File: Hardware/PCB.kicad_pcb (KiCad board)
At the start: 2 copper layers, 53.4 x 22 mm, 13 parts, among them J2 Conn_01x06, SW1 SW_MEC_5E, U1 ME54BS01_V1.0, U2 MCP1700x-330xxTO

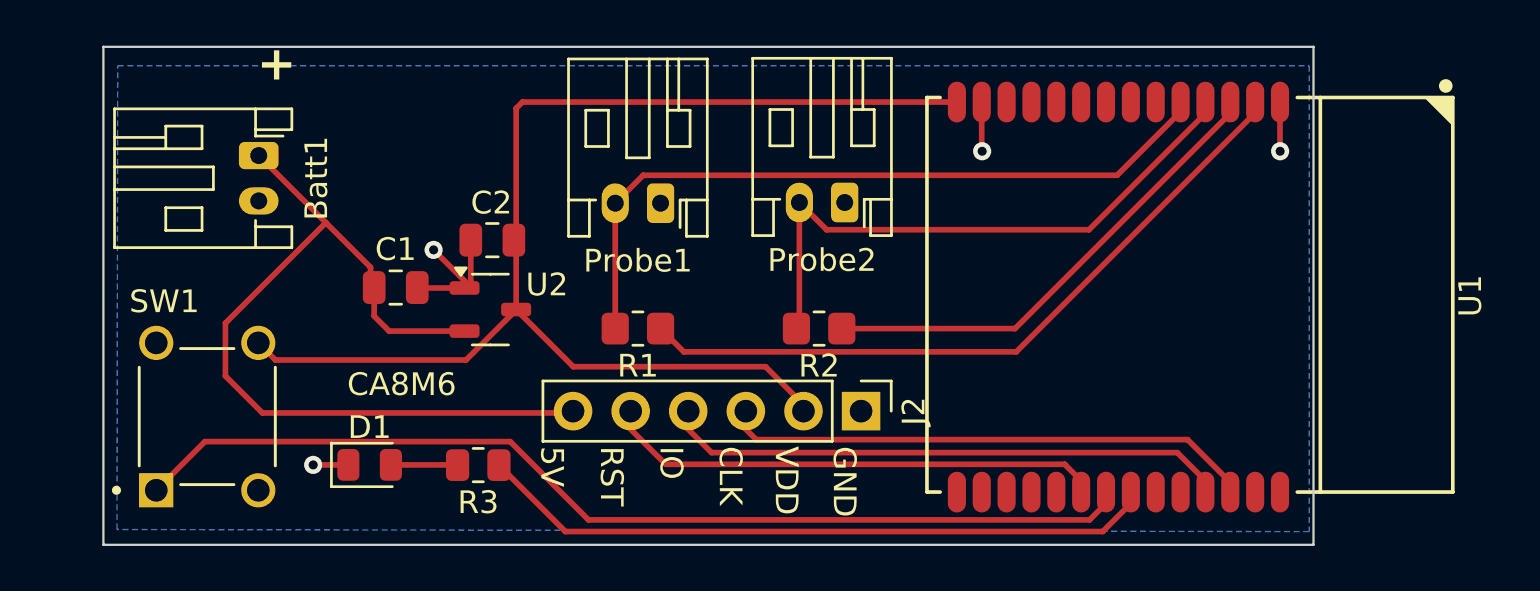
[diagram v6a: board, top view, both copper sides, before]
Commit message: Update PCB with fix for LDO and tracing improvements.
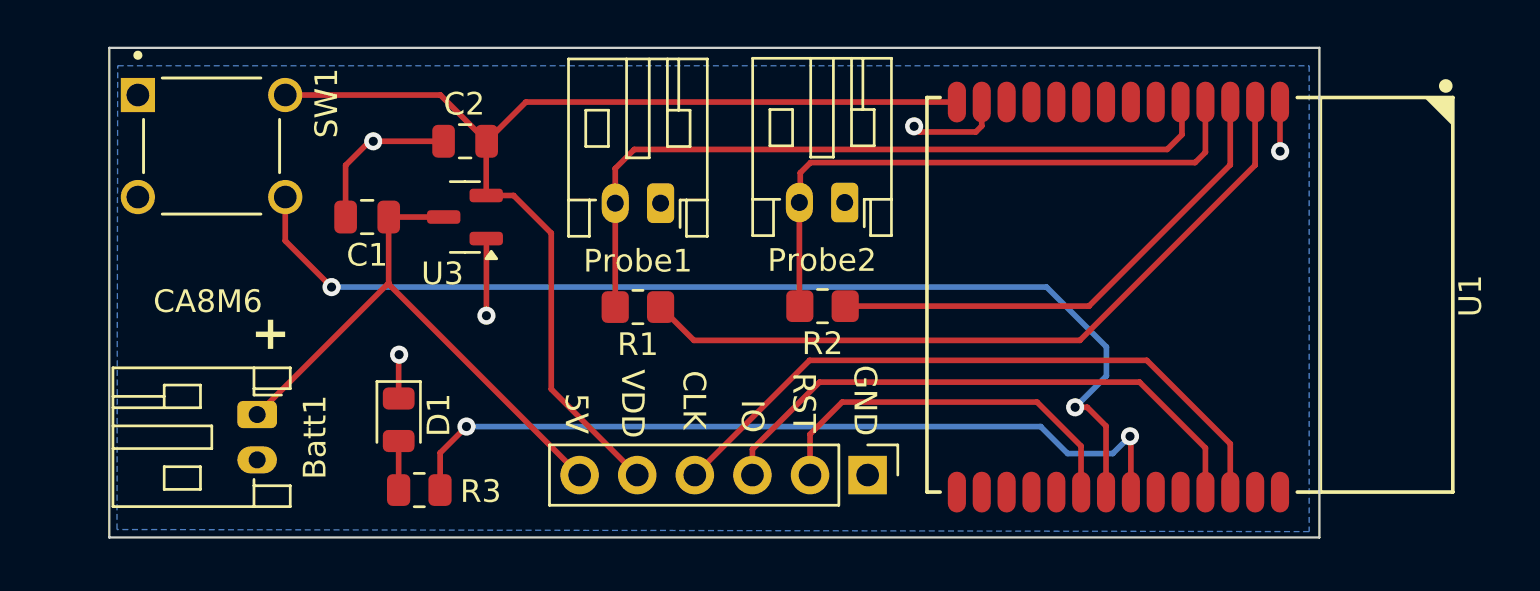
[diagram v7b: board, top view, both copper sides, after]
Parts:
- removed U2: MCP1700x-330xxTO, Package_TO_SOT_SMD:SOT-23-3
- added U3: MCP1700x-330xxTT, Package_TO_SOT_SMD:SOT-23, F.Cu at (56.9, 62.8)
- moved SW1 11.9 mm to (45.7, 59.7), turned to 0 degrees
- moved Batt1 11.4 mm to (47.7, 71.5)
- moved C2 4.52 mm to (56.9, 59.5)
- moved C1 3.36 mm to (52.6, 62.8), turned to 180 degrees
- moved J2 2.83 mm to (74.6, 74.2)
- moved R3 2.82 mm to (54.9, 74.8)
- moved D1 2.37 mm to (54.0, 71.8), turned to -90 degrees
- moved R2 1.00 mm to (72.6, 66.7)
- moved R1 0.95 mm to (64.5, 66.8)
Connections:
- C2 pad 1: Net-(J2-Pin_2) -> Net-(J2-Pin_5)
- SW1 pad 1: Net-(U1-P2.09) -> unconnected-(SW1-Pad1)
- SW1 pad 2: unconnected-(SW1-Pad2) -> Net-(J2-Pin_5)
- SW1 pad 4: Net-(J2-Pin_2) -> Net-(SW1-A)
- U1 pad 14: Net-(J2-Pin_2) -> Net-(J2-Pin_5)
- U1 pad 20: Net-(J2-Pin_5) -> Net-(J2-Pin_2)
- U1 pad 21: Net-(U1-P2.09) -> Net-(SW1-A)
- U1 pad 25: Net-(J2-Pin_4) -> Net-(J2-Pin_3)
- U1 pad 26: Net-(J2-Pin_3) -> Net-(J2-Pin_4)
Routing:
- net Net-(SW1-A): track 0.00 -> 48.4 mm, vias 0 -> 2
- net Net-(U1-P2.09): track 45.5 -> 0.00 mm
- net Net-(J2-Pin_2): track 55.7 -> 17.2 mm
- net Net-(J2-Pin_5): track 22.3 -> 49.4 mm
- net Net-(Batt1-Pin_1): track 37.3 -> 25.5 mm
- net GND: track 13.1 -> 19.5 mm, vias 4 -> 5
- net Net-(U1-P2.10): track 30.6 -> 36.3 mm, vias 0 -> 2
- net Net-(J2-Pin_4): track 25.8 -> 29.8 mm
- net Net-(J2-Pin_3): track 24.3 -> 26.6 mm
- net Net-(U1-P1.09): track 32.0 -> 32.8 mm
- net Net-(U1-P1.10): track 21.6 -> 22.3 mm
- net Net-(D1-A): track 2.84 -> 2.16 mm
- net Net-(Probe1-Pin_2): track 33.1 -> 33.7 mm
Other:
- board size 53.4 x 22 mm -> 53.4 x 21.6 mm

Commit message: Revision 2 of the PCB using all SMD components
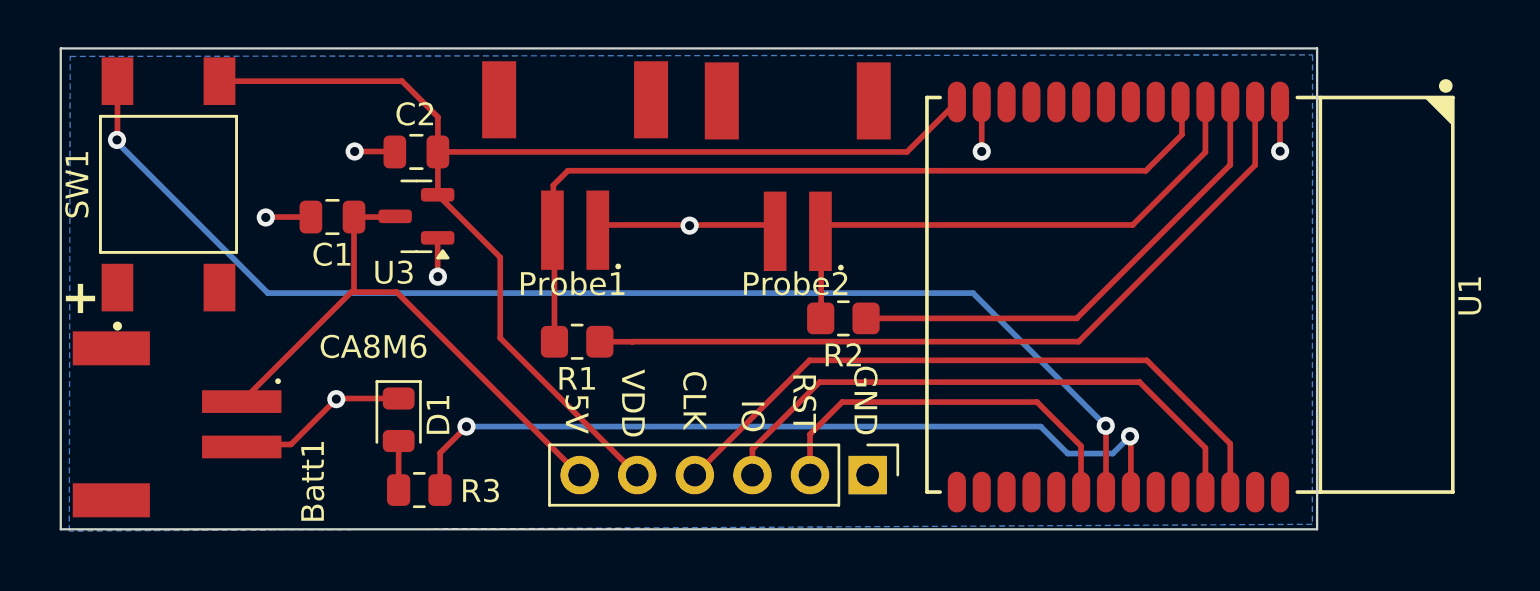
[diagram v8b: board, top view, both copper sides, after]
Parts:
- Batt1, Probe1, Probe2: footprint Connector_JST:JST_PH_S2B-PH-K_1x02_P2.00mm_Horizontal -> S2B-PH-SM4-TB:JST_S2B-PH-SM4-TB
- SW1: value SW_MEC_5E -> TS04-66-43-BK-100-SMT; footprint TS02-66-55-BK-100-LCR-D:SW_TS02-66-55-BK-100-LCR-D -> TS04-66-43-BK-100-SMT:SW_TS04-66-43-BK-100-SMT
- moved Probe1 3.95 mm to (61.7, 63.4), turned to 0 degrees
- moved R1 3.09 mm to (61.8, 68.3)
- moved SW1 2.54 mm to (43.8, 61.4), turned to 90 degrees
- moved Probe2 2.43 mm to (71.5, 63.4), turned to 0 degrees
- moved C2 2.20 mm to (54.7, 59.9)
- moved U3 2.14 mm to (54.7, 62.8)
- moved C1 1.53 mm to (51.0, 62.8)
- moved R2 1.07 mm to (73.6, 67.3)
- moved Batt1 0.80 mm to (47.0, 72.0), turned to 90 degrees
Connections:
- Probe2 pad 1: GND -> Net-(Probe2-Pin_1)
- Probe2 pad 2: Net-(Probe2-Pin_2) -> GND
- R2 pad 2: Net-(Probe2-Pin_2) -> Net-(Probe2-Pin_1)
- SW1 pad 2: Net-(J2-Pin_5) -> unconnected-(SW1-Pad2)
- SW1 pad 3: unconnected-(SW1-K-Pad3) -> Net-(U1-P2.09)
- SW1 pad 4: Net-(SW1-A) -> Net-(J2-Pin_5)
- U1 pad 21: Net-(SW1-A) -> Net-(U1-P2.09)
- U1 pad 4: Net-(Probe2-Pin_2) -> Net-(Probe2-Pin_1)
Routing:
- net Net-(U1-P2.09): track 0.00 -> 54.4 mm, vias 0 -> 2
- net Net-(SW1-A): track 48.4 -> 0.00 mm, vias 2 -> 0
- net Net-(Probe2-Pin_2): track 26.9 -> 0.00 mm
- net Net-(Probe2-Pin_1): track 0.00 -> 23.9 mm
- net GND: track 19.5 -> 25.2 mm, vias 5 -> 7
- net Net-(J2-Pin_5): track 49.4 -> 53.5 mm
- net Net-(Probe1-Pin_2): track 33.7 -> 37.0 mm
- net Net-(U1-P1.09): track 32.8 -> 34.9 mm
- net Net-(U1-P1.10): track 22.3 -> 21.6 mm
- net Net-(U1-P2.10): track 36.3 -> 35.8 mm
- net unconnected-(U1-P1.05/AIN1-Pad9): track 0.50 -> 0.00 mm
- net unconnected-(U1-P1.04/AIN0-Pad12): track 0.50 -> 0.00 mm
- net Net-(J2-Pin_3): track 26.6 -> 26.1 mm
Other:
- board size 53.4 x 21.6 mm -> 55.4 x 21.2 mm
